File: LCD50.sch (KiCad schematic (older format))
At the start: 38 parts, among them Q10 IRLML2502, Q8 IRLML2502, Q9 IRLML2502, U20 xc7z020clg484

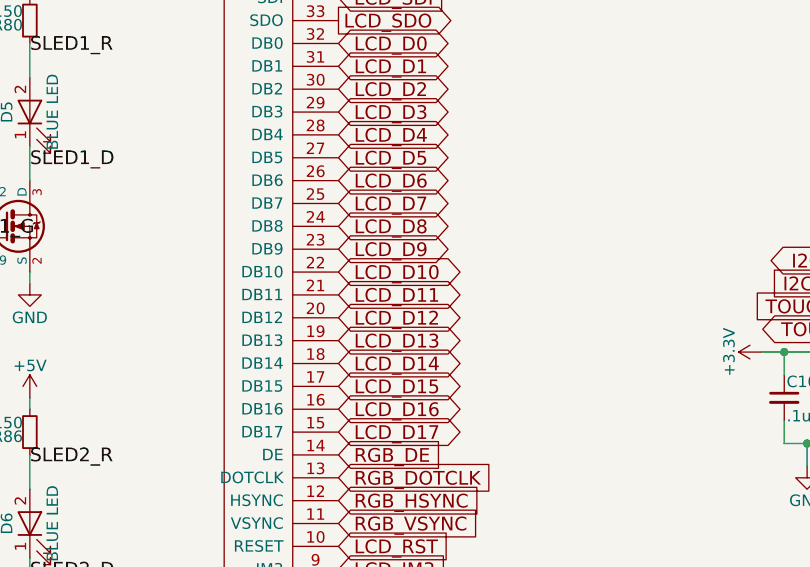
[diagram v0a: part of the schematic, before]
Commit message: widened serpentine routing consistant with guidelines (3x trace-to-plane) need to do data byte 2 and all address lines
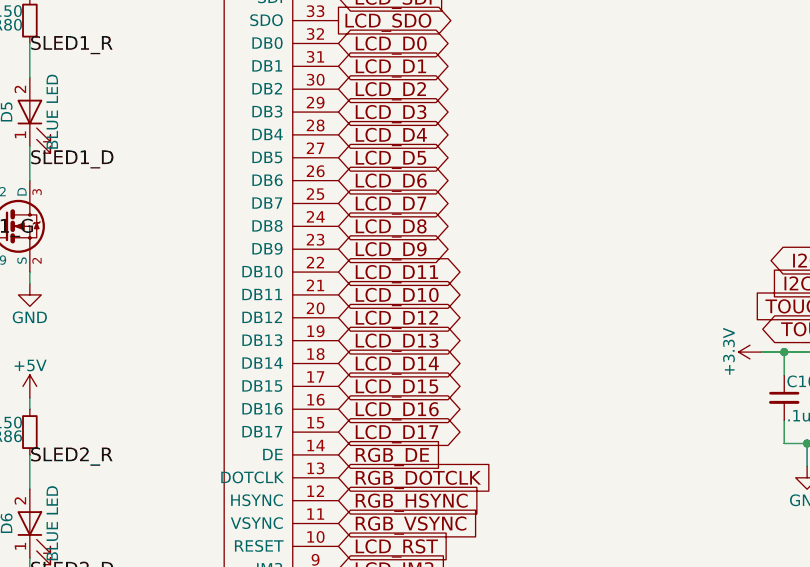
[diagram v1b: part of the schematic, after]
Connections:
- net LCD_D10: now also CONN2.21 (DB11); no longer CONN2.22 (DB10)
- net LCD_D11: now also CONN2.22 (DB10); no longer CONN2.21 (DB11)
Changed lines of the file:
@@
 Text GLabel 2650 5100 2    60   BiDi ~ 0
 LCD_D9
+Text GLabel 2650 5300 2    60   BiDi ~ 0
+LCD_D10
 Text GLabel 2650 5200 2    60   BiDi ~ 0
-LCD_D10
-Text GLabel 2650 5300 2    60   BiDi ~ 0
 LCD_D11
 Text GLabel 2650 5400 2    60   BiDi ~ 0

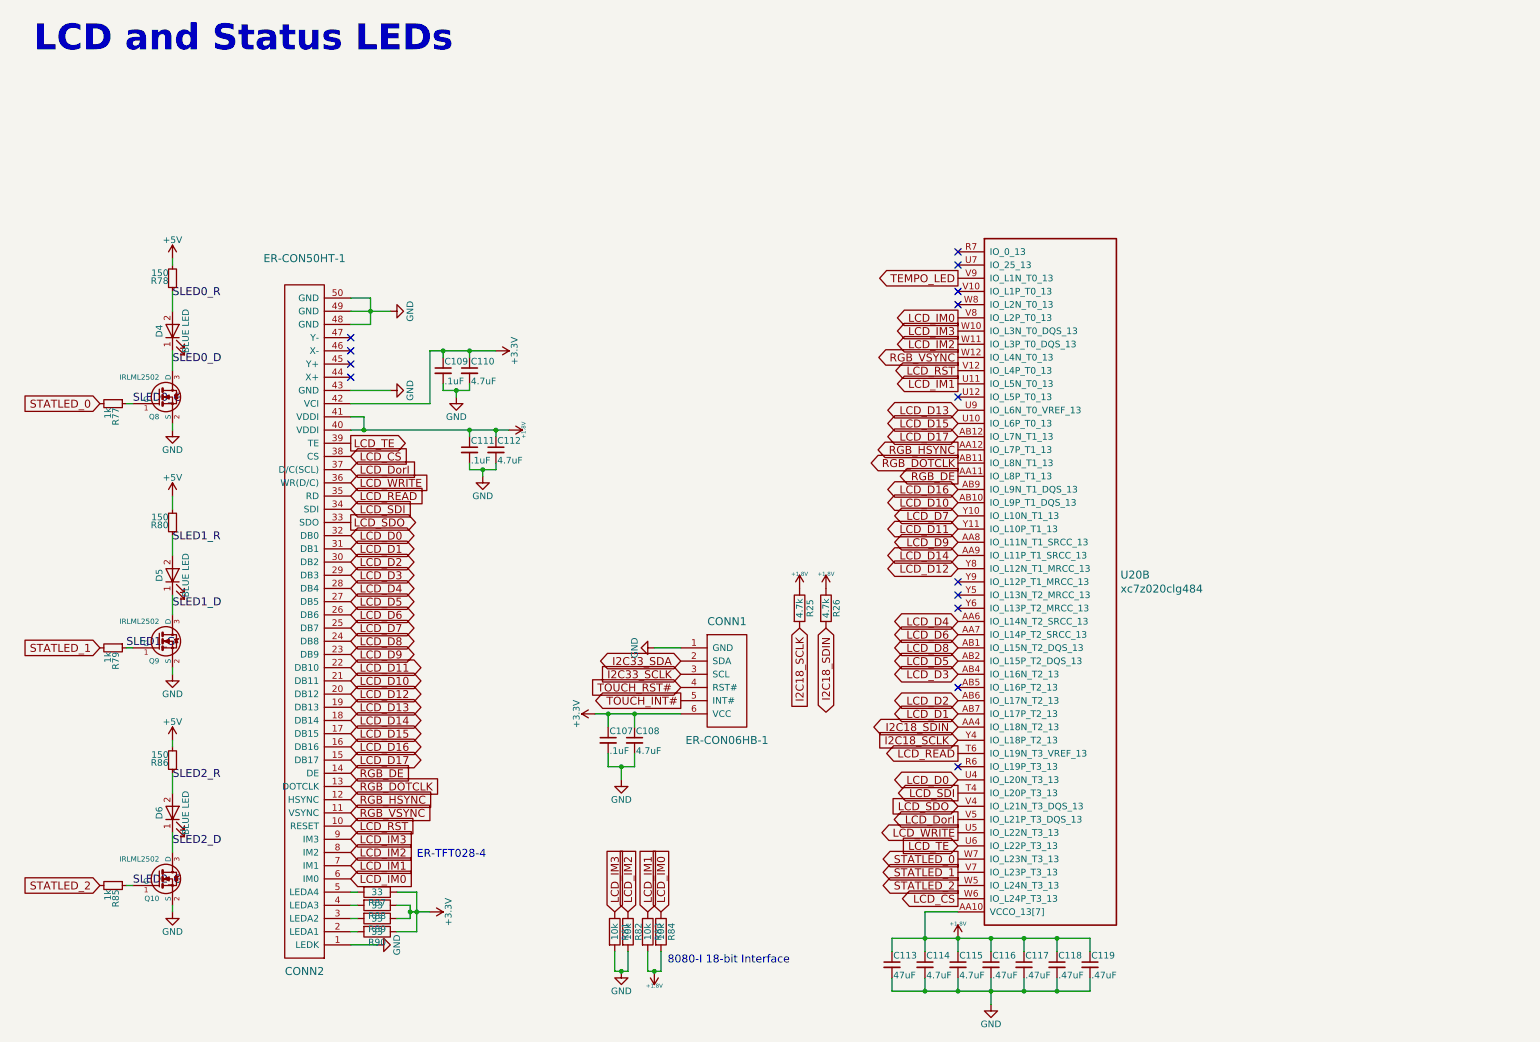
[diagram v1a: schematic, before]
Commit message: about to remove ZIF screen connector in favor of UNO + RPI
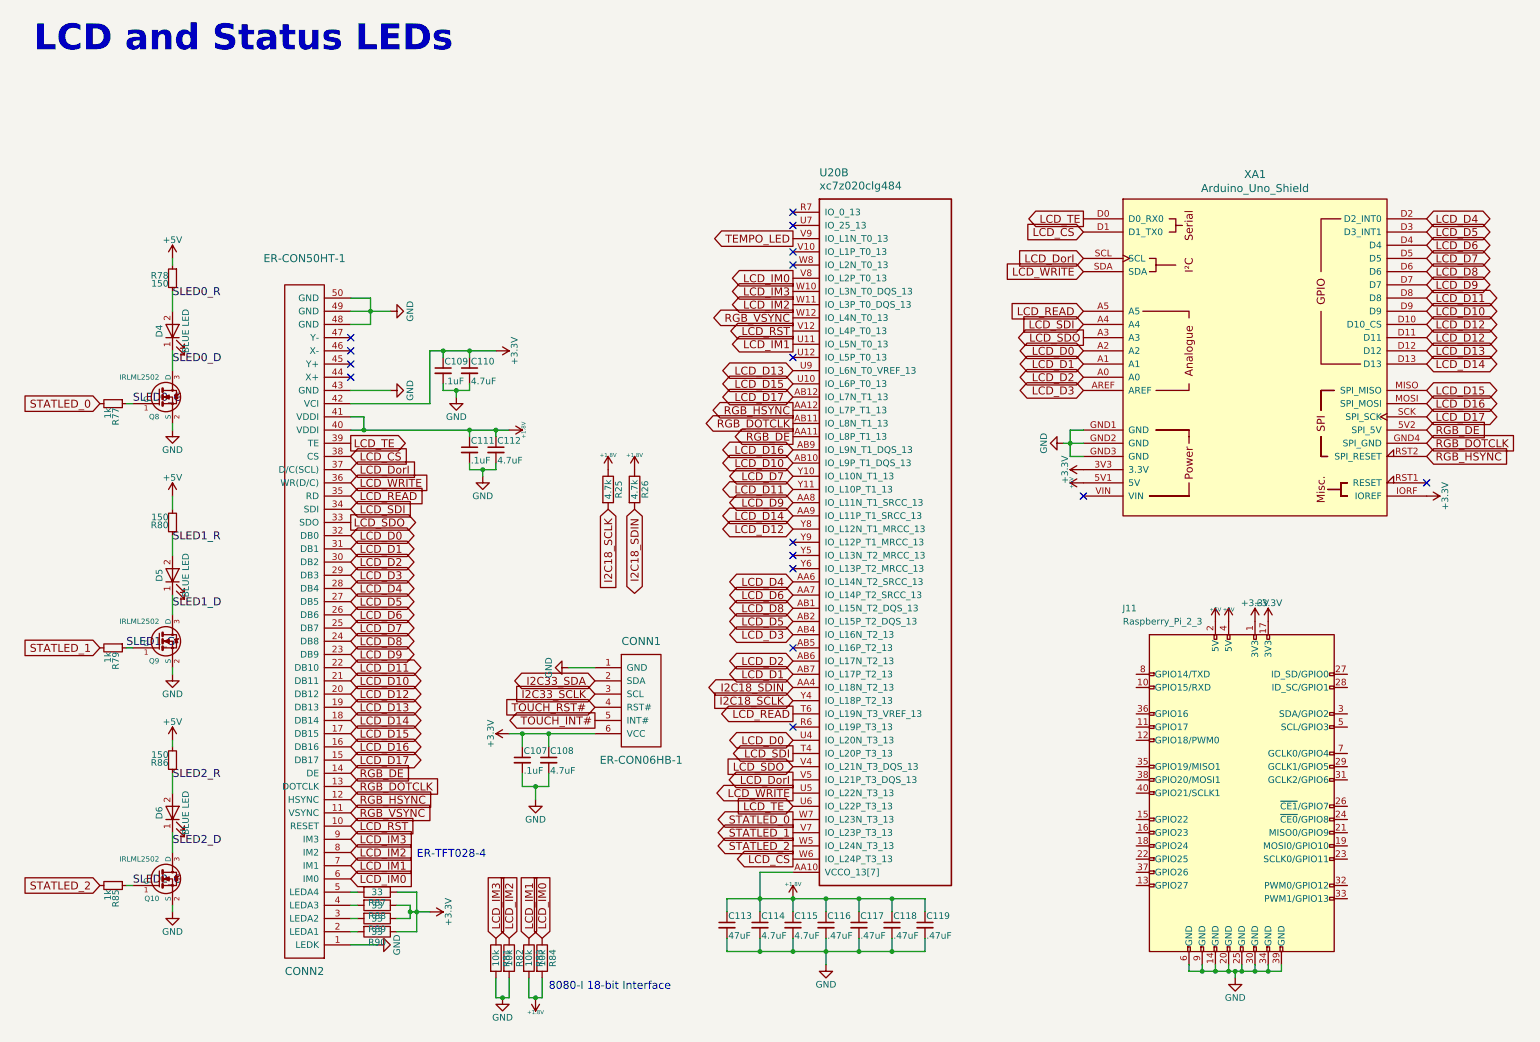
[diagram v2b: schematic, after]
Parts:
- added J11: Raspberry_Pi_2_3, Connector_PinSocket_2.54mm:PinSocket_2x20_P2.54mm_Horizontal, symbol Connector:Raspberry_Pi_2_3
- added XA1: Arduino_Uno_Shield, DFTcustom:Arduino_Uno_Shield, symbol arduino:Arduino_Uno_Shield
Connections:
- net +3V3: now also J11.1 (3V3), J11.17 (3V3), XA1.3V3 (3.3V), XA1.IORF (IOREF)
- net +5V: now also R78.1, J11.2 (5V), J11.4 (5V), XA1.5V1 (5V); no longer R78.2
- net GND: now also J11.14 (GND), J11.20 (GND), J11.25 (GND), J11.30 (GND), J11.34 (GND), J11.39 (GND), J11.6 (GND), J11.9 (GND), XA1.GND1 (GND), XA1.GND2 (GND), XA1.GND3 (GND)
- net LCD_CS: now also XA1.D1 (D1_TX0)
- net LCD_D0: now also XA1.A2
- net LCD_D1: now also XA1.A1
- net LCD_D10: now also XA1.D9
- net LCD_D11: now also XA1.D8
- net LCD_D12: now also XA1.D10 (D10_CS), XA1.D11
- net LCD_D13: now also XA1.D12
- net LCD_D14: now also XA1.D13
- net LCD_D15: now also XA1.MISO (SPI_MISO)
- net LCD_D16: now also XA1.MOSI (SPI_MOSI)
- net LCD_D17: now also XA1.SCK (SPI_SCK)
- net LCD_D2: now also XA1.A0
- net LCD_D3: now also XA1.AREF
- net LCD_D4: now also XA1.D2 (D2_INT0)
- net LCD_D5: now also XA1.D3 (D3_INT1)
- net LCD_D6: now also XA1.D4
- net LCD_D7: now also XA1.D5
- net LCD_D8: now also XA1.D6
- net LCD_D9: now also XA1.D7
- net LCD_DorI: now also XA1.SCL
- net LCD_READ: now also XA1.A5
- net LCD_SDI: now also XA1.A4
- net LCD_SDO: now also XA1.A3
- net LCD_TE: now also XA1.D0 (D0_RX0)
- net LCD_WRITE: now also XA1.SDA
- net RGB_DE: now also XA1.5V2 (SPI_5V)
- net RGB_DOTCLK: now also XA1.GND4 (SPI_GND)
- net RGB_HSYNC: now also XA1.RST2 (SPI_RESET)
- net SLED0_R: now also R78.2; no longer R78.1
- no-connect marks 14 -> 16
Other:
- moved on the sheet: C107, C108, C113, C114, C115, C116, C117, C118, C119, CONN1, R25, R26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

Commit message: added arduino header, shifted components, deleted 50pin ZIF, deleted MIDI in for fear of confusion with headphone jack
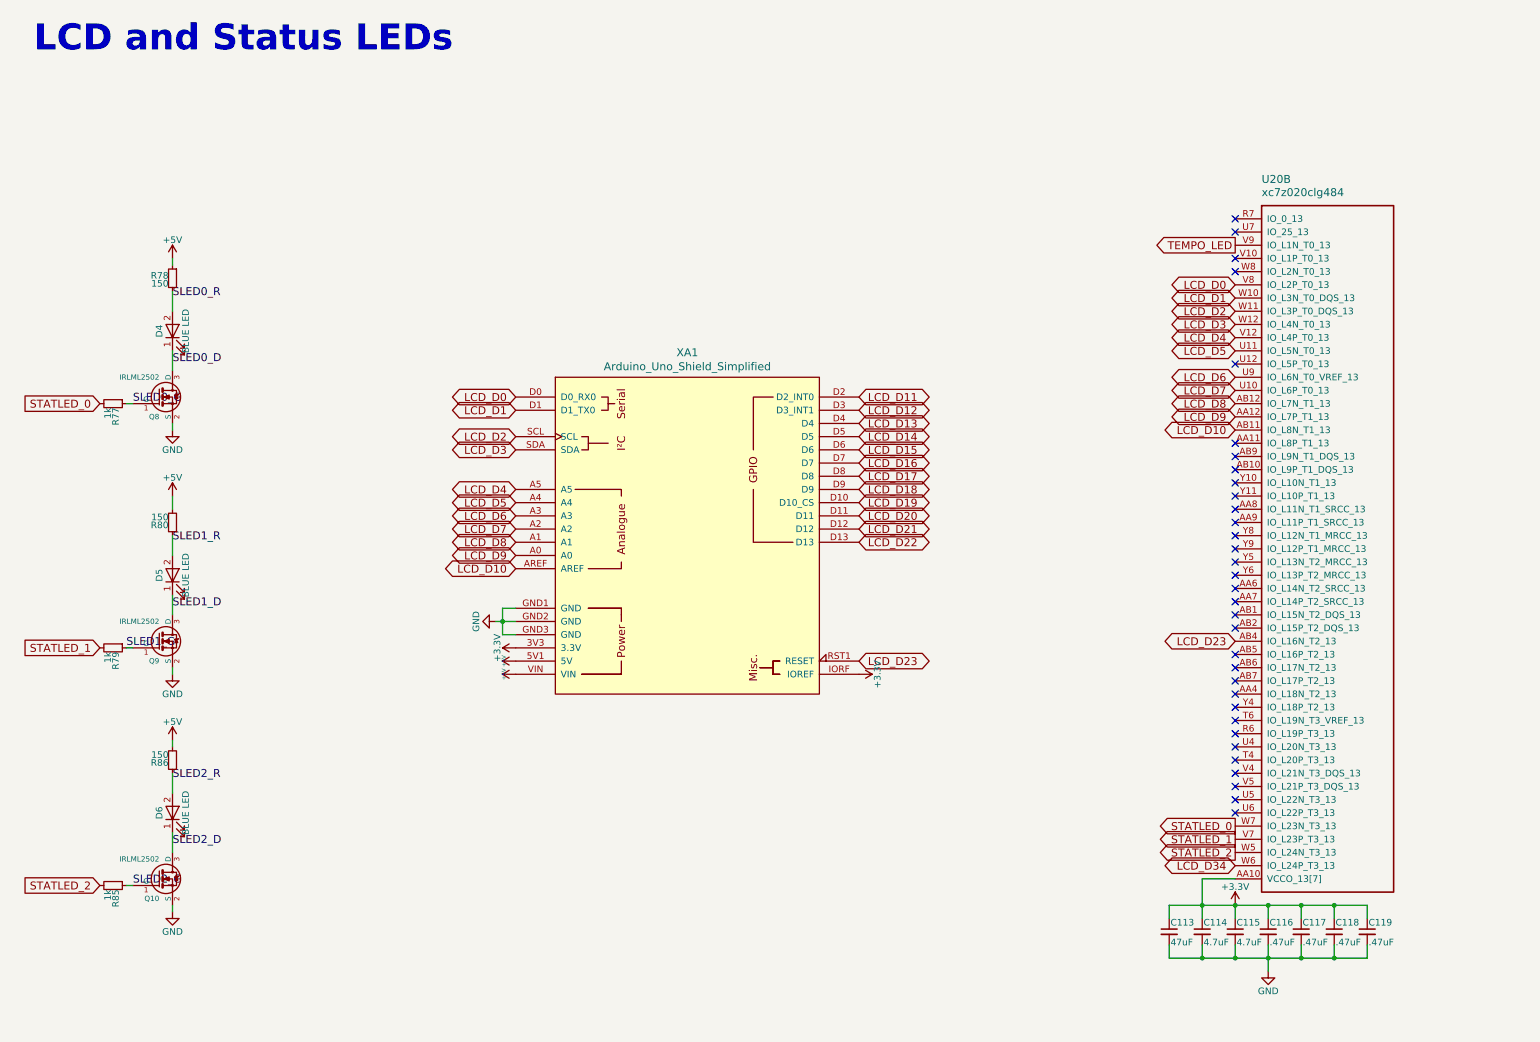
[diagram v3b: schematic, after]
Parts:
- removed C107, C109, C111: .1uF, Capacitor_SMD:C_0402_1005Metric, symbol Device:C_Small
- removed C108, C110, C112: 4.7uF, Capacitor_SMD:C_0402_1005Metric, symbol Device:C_Small
- removed CONN1: ER-CON06HB-1, DFTcustom:ER-CON06HB-1, symbol DFTBoard-rescue:ER-CON06HB-1-
- removed CONN2: ER-CON50HT-1, DFTcustom:ER-CON50HT-1, symbol DFTBoard-rescue:ER-CON50HT-1-
- removed J11: Raspberry_Pi_2_3, Connector_PinSocket_2.54mm:PinSocket_2x20_P2.54mm_Horizontal, symbol Connector:Raspberry_Pi_2_3
- removed R25, R26: 4.7k, Resistor_SMD:R_0402_1005Metric, symbol Device:R
- removed R81, R82, R83, R84: 10k, Resistor_SMD:R_0402_1005Metric, symbol Device:R
- removed R87, R88, R89, R90: 33, Resistor_SMD:R_0402_1005Metric, symbol Device:R
- removed XA1: Arduino_Uno_Shield, DFTcustom:Arduino_Uno_Shield, symbol arduino:Arduino_Uno_Shield
- added XA1: Arduino_Uno_Shield_Simplified, DFTcustom:Arduino_Uno_Shield_Simplified, symbol arduino:Arduino_Uno_Shield_Simplified
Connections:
- net +1V8 is gone; now on net +3V3: C113.1, C114.1, C115.1, C116.1, C117.1, C118.1, C119.1, U20.AA10 (VCCO_13[7]), U20.AB3 (VCCO_13[7]), U20.T5 (VCCO_13[7]), U20.U8 (VCCO_13[7]), U20.V11 (VCCO_13[7]), U20.W4 (VCCO_13[7]), U20.Y7 (VCCO_13[7])
- net LCD_IM0 is gone; now on net LCD_D0: U20.V8 (IO_L2P_T0_13)
- net LCD_IM1 is gone; now on net LCD_D5: U20.U11 (IO_L5N_T0_13)
- net LCD_IM2 is gone; now on net LCD_D2: U20.W11 (IO_L3P_T0_DQS_13)
- net LCD_IM3 is gone; now on net LCD_D1: U20.W10 (IO_L3N_T0_DQS_13)
- net LCD_RST is gone; now on net LCD_D4: U20.V12 (IO_L4P_T0_13)
- net RGB_DOTCLK is gone; now on net LCD_D10: U20.AB11 (IO_L8N_T1_13)
- net RGB_HSYNC is gone; now on net LCD_D9: U20.AA12 (IO_L7P_T1_13)
- net RGB_VSYNC is gone; now on net LCD_D3: U20.W12 (IO_L4N_T0_13)
- net +3V3: now also XA1.3V3 (3.3V), XA1.IORF (IOREF)
- net +5V: now also XA1.5V1 (5V), XA1.VIN
- net GND: now also XA1.GND1 (GND), XA1.GND2 (GND), XA1.GND3 (GND)
- net LCD_D0: now also XA1.D0 (D0_RX0); no longer U20.U4 (IO_L20N_T3_13)
- net LCD_D1: now also XA1.D1 (D1_TX0); no longer U20.AB7 (IO_L17P_T2_13)
- net LCD_D10: now also XA1.AREF; no longer U20.AB10 (IO_L9P_T1_DQS_13)
- net LCD_D11: now also XA1.D2 (D2_INT0); no longer U20.Y11 (IO_L10P_T1_13)
- net LCD_D12: now also XA1.D3 (D3_INT1); no longer U20.Y8 (IO_L12N_T1_MRCC_13)
- net LCD_D13: now also XA1.D4; no longer U20.U9 (IO_L6N_T0_VREF_13)
- net LCD_D14: now also XA1.D5; no longer U20.AA9 (IO_L11P_T1_SRCC_13)
- net LCD_D15: now also XA1.D6; no longer U20.U10 (IO_L6P_T0_13)
- net LCD_D16: now also XA1.D7; no longer U20.AB9 (IO_L9N_T1_DQS_13)
- net LCD_D17: now also XA1.D8; no longer U20.AB12 (IO_L7N_T1_13)
- net LCD_D2: now also XA1.SCL; no longer U20.AB6 (IO_L17N_T2_13)
- net LCD_D3: now also XA1.SDA; no longer U20.AB4 (IO_L16N_T2_13)
- net LCD_D4: now also XA1.A5; no longer U20.AA6 (IO_L14N_T2_SRCC_13)
- net LCD_D5: now also XA1.A4; no longer U20.AB2 (IO_L15P_T2_DQS_13)
- net LCD_D6: now also U20.U9 (IO_L6N_T0_VREF_13), XA1.A3; no longer U20.AA7 (IO_L14P_T2_SRCC_13)
- net LCD_D7: now also U20.U10 (IO_L6P_T0_13), XA1.A2; no longer U20.Y10 (IO_L10N_T1_13)
- net LCD_D8: now also U20.AB12 (IO_L7N_T1_13), XA1.A1; no longer U20.AB1 (IO_L15N_T2_DQS_13)
- net LCD_D9: now also XA1.A0; no longer U20.AA8 (IO_L11N_T1_SRCC_13)
- net I2C18_SCLK: no longer names the net of U20.Y4 (IO_L18P_T2_13)
- net I2C18_SDIN: no longer names the net of U20.AA4 (IO_L18N_T2_13)
- net LCD_CS renamed LCD_D34
- net LCD_DorI: no longer names the net of U20.V5 (IO_L21P_T3_DQS_13)
- net LCD_READ: no longer names the net of U20.T6 (IO_L19N_T3_VREF_13)
- net LCD_SDI: no longer names the net of U20.T4 (IO_L20P_T3_13)
- net LCD_SDO: no longer names the net of U20.V4 (IO_L21N_T3_DQS_13)
- net LCD_TE: no longer names the net of U20.U6 (IO_L22P_T3_13)
- net LCD_WRITE: no longer names the net of U20.U5 (IO_L22N_T3_13)
- net RGB_DE: no longer names the net of U20.AA11 (IO_L8P_T1_13)
- new net LCD_D18: XA1.D9
- new net LCD_D19: XA1.D10 (D10_CS)
- new net LCD_D20: XA1.D11
- new net LCD_D21: XA1.D12
- new net LCD_D22: XA1.D13
- new net LCD_D23: U20.AB4 (IO_L16N_T2_13), XA1.RST1 (RESET)
- no-connect marks 16 -> 33
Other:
- note removed: "8080-I 18-bit Interface"
- note removed: "ER-TFT028-4"
- moved on the sheet: C113, C114, C115, C116, C117, C118, C119, U20B
